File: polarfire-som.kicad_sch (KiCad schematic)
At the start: 0 parts

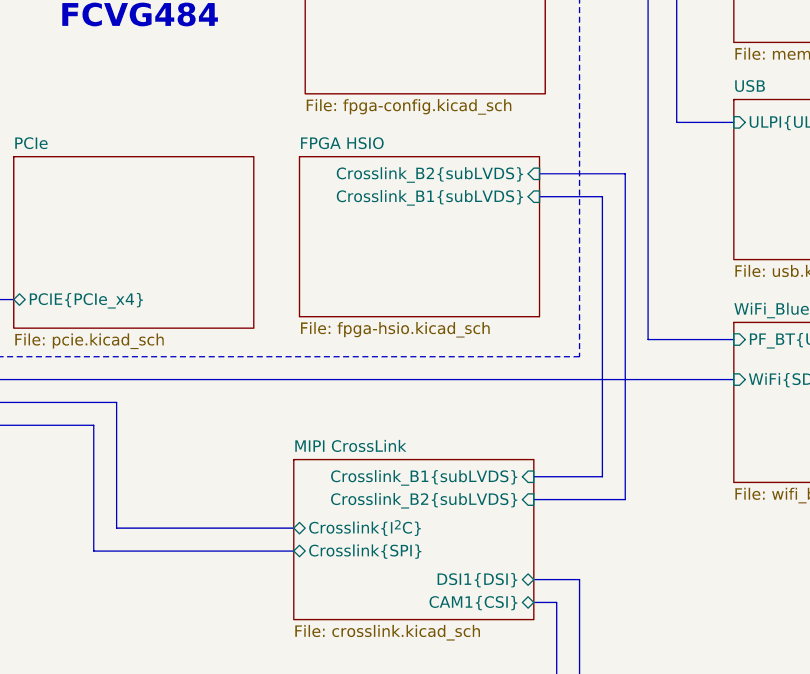
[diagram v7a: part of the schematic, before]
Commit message: [#57878] Fix power planes and bus naming
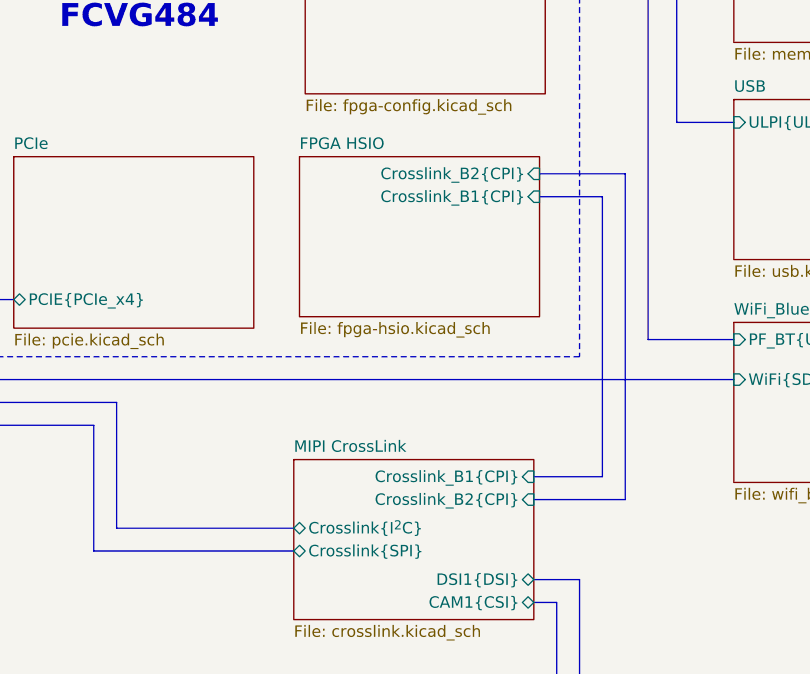
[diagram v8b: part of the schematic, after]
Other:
- sheet FPGA HSIO ports: added Crosslink_B1{CPI}, Crosslink_B2{CPI}; removed Crosslink_B1{subLVDS}, Crosslink_B2{subLVDS}
- sheet MIPI CrossLink ports: added Crosslink_B1{CPI}, Crosslink_B2{CPI}; removed Crosslink_B1{subLVDS}, Crosslink_B2{subLVDS}
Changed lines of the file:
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@@
       (effects (font (size 1.27 1.27)) (justify left top))
     )
-    (pin "Crosslink_B1{subLVDS}" input (at 262.255 146.05 0)
+    (pin "Crosslink_B1{CPI}" input (at 262.255 146.05 0)
       (effects (font (size 1.27 1.27)) (justify right))
     )
-    (pin "Crosslink_B2{subLVDS}" input (at 262.255 143.51 0)
+    (pin "Crosslink_B2{CPI}" input (at 262.255 143.51 0)
       (effects (font (size 1.27 1.27)) (justify right))
     )
@@
       (effects (font (size 1.27 1.27)) (justify right))
     )
-    (pin "Crosslink_B1{subLVDS}" input (at 261.62 177.165 0)
+    (pin "Crosslink_B1{CPI}" input (at 261.62 177.165 0)
       (effects (font (size 1.27 1.27)) (justify right))
     )
-    (pin "Crosslink_B2{subLVDS}" input (at 261.62 179.705 0)
+    (pin "Crosslink_B2{CPI}" input (at 261.62 179.705 0)
       (effects (font (size 1.27 1.27)) (justify right))
     )
